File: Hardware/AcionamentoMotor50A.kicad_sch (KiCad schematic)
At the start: 56 parts, among them J1 Conn_01x02, J2 Conn_01x02, J3 Conn_01x02, Q1 IXFN420N10T, Q2 IXFN420N10T, Q3 IXFN420N10T, Q4 IXFN420N10T, U1 IXFN420N10T

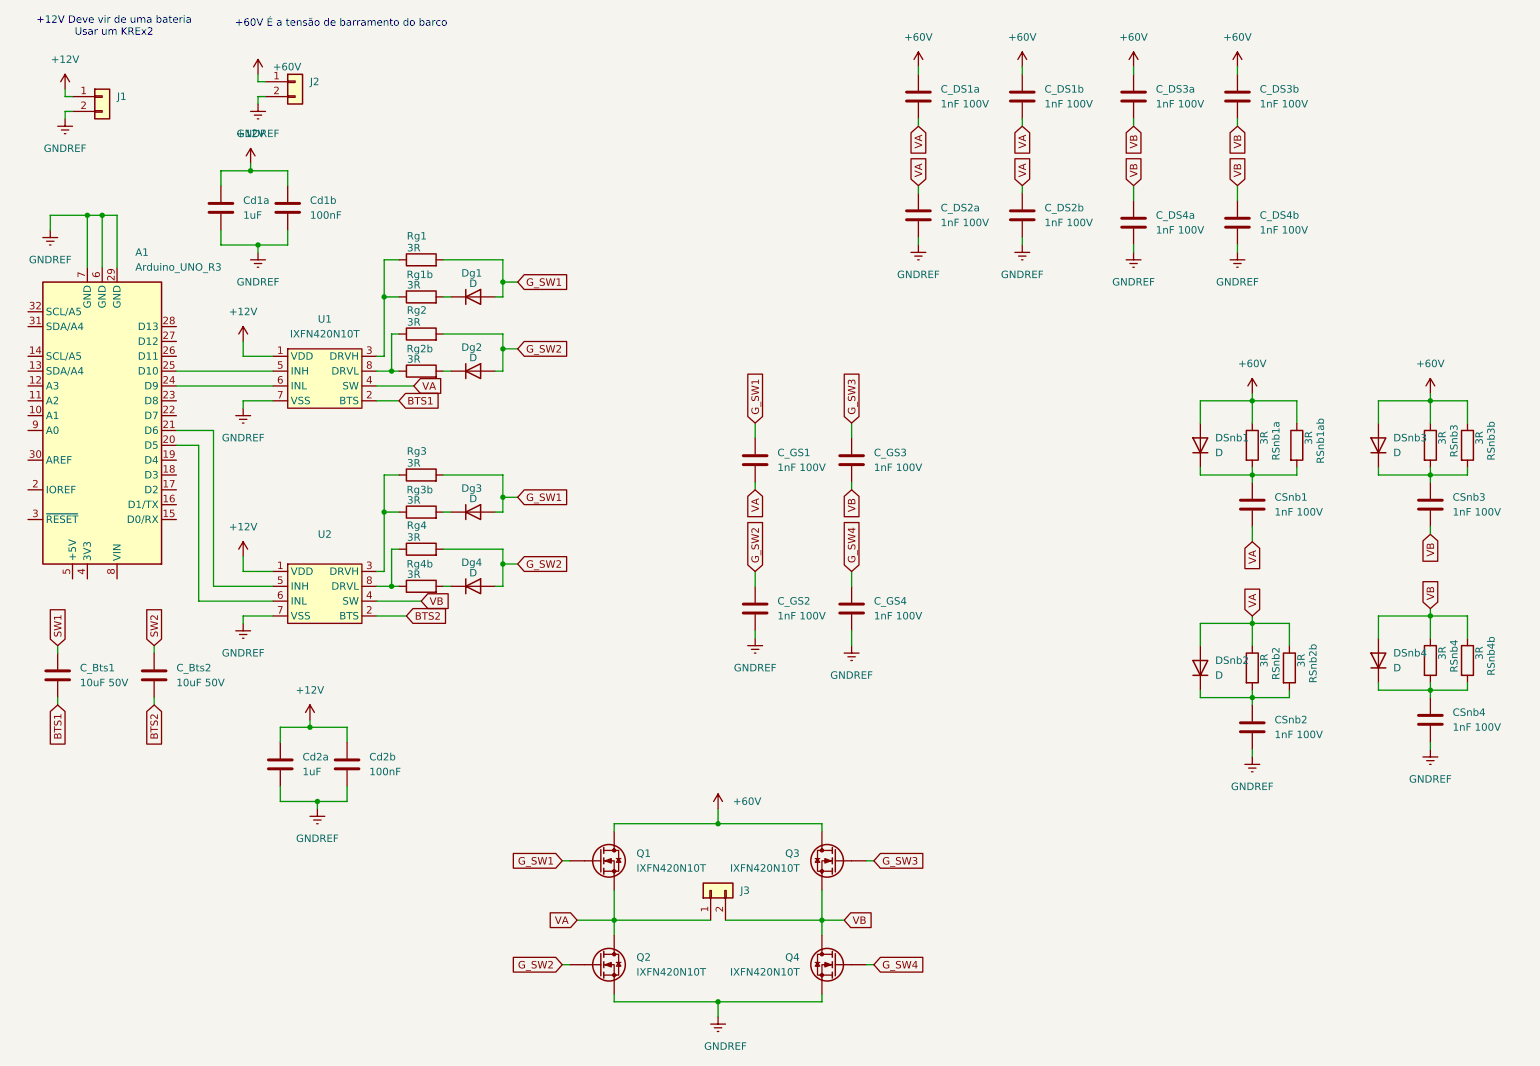
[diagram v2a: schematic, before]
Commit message: 2026_06_25
Esquemático finalizado.

Footprints corrigidos
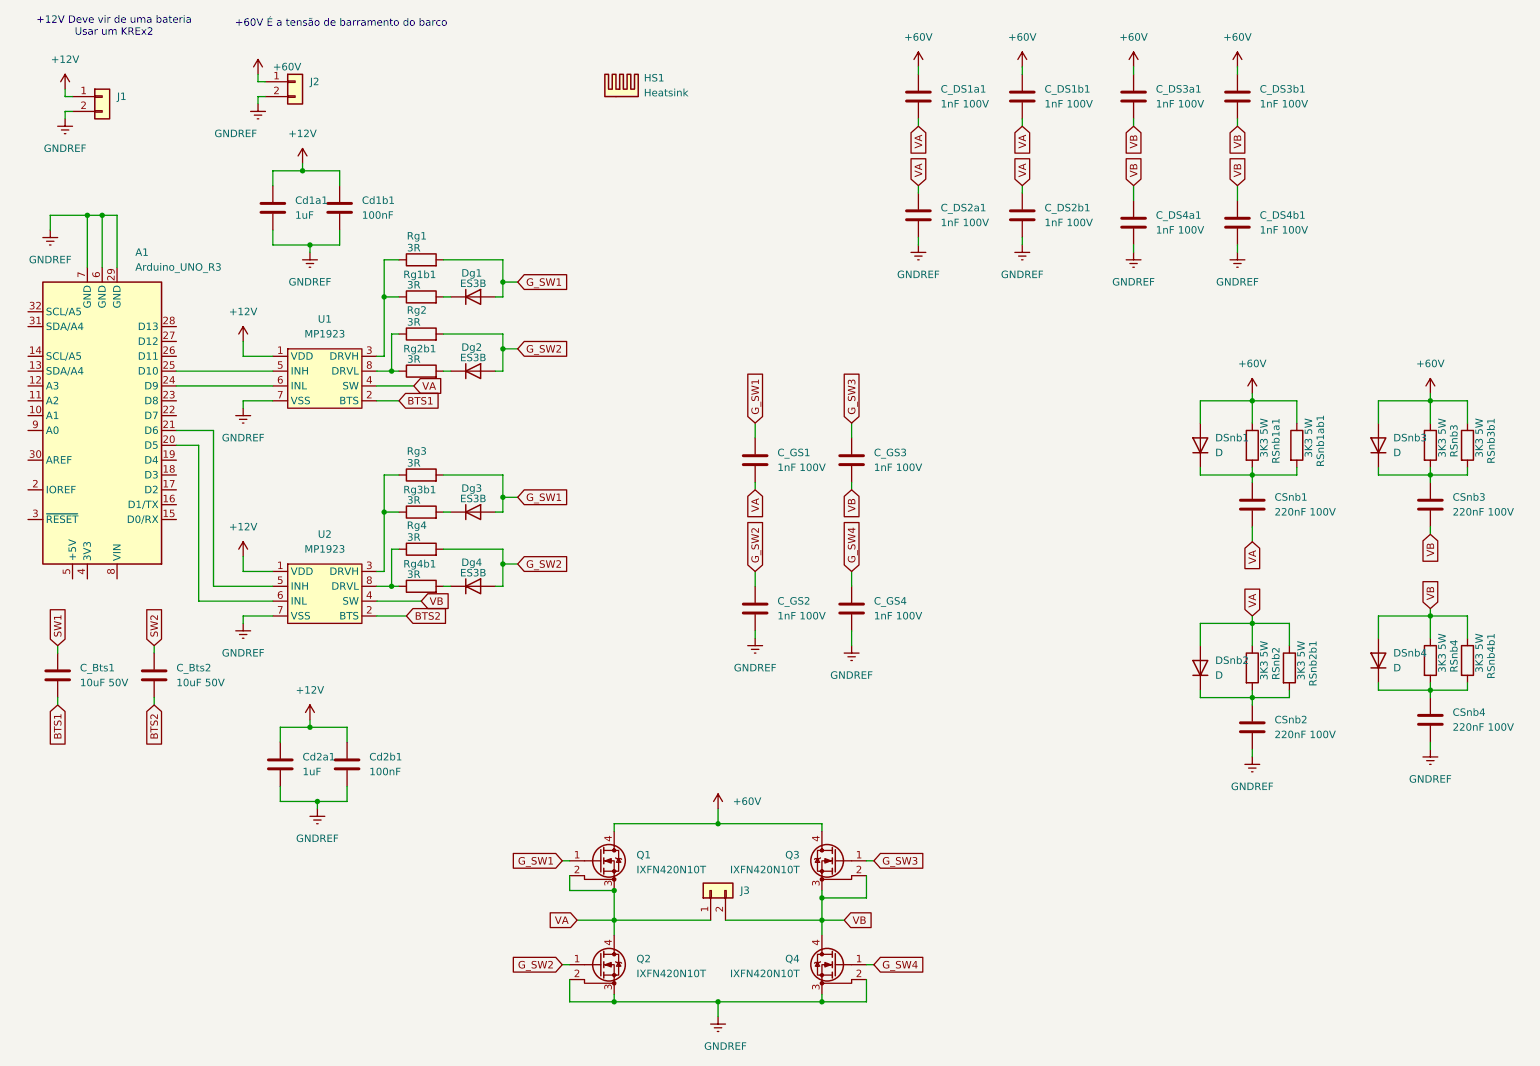
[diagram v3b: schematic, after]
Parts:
- removed Q1, Q2, Q3, Q4: IXFN420N10T, symbol Device:Q_NMOS
- added HS1: Heatsink, ZeniteSolar:Heatsink_120mmx100mm_H70mm, symbol Mechanical:Heatsink
- added Q1, Q2, Q3, Q4: IXFN420N10T, ZeniteSolar:SOT-227, symbol ZeniteSolar:IXFN420N10T
- CSnb1, CSnb2, CSnb3, CSnb4: value 1nF 100V -> 220nF 100V; footprint (none) -> Capacitor_THT:C_Axial_L5.1mm_D3.1mm_P10.00mm_Horizontal
- C_Bts1, C_Bts2, C_GS1, C_GS2, C_GS3, C_GS4: footprint (none) -> Capacitor_SMD:C_0805_2012Metric_Pad1.18x1.45mm_HandSolder
- C_DS1a1: renamed from C_DS1a; footprint (none) -> Capacitor_SMD:C_0805_2012Metric_Pad1.18x1.45mm_HandSolder
- C_DS1b1: renamed from C_DS1b; footprint (none) -> Capacitor_SMD:C_0805_2012Metric_Pad1.18x1.45mm_HandSolder
- C_DS2a1: renamed from C_DS2a; footprint (none) -> Capacitor_SMD:C_0805_2012Metric_Pad1.18x1.45mm_HandSolder
- C_DS2b1: renamed from C_DS2b; footprint (none) -> Capacitor_SMD:C_0805_2012Metric_Pad1.18x1.45mm_HandSolder
- C_DS3a1: renamed from C_DS3a; footprint (none) -> Capacitor_SMD:C_0805_2012Metric_Pad1.18x1.45mm_HandSolder
- C_DS3b1: renamed from C_DS3b; footprint (none) -> Capacitor_SMD:C_0805_2012Metric_Pad1.18x1.45mm_HandSolder
- C_DS4a1: renamed from C_DS4a; footprint (none) -> Capacitor_SMD:C_0805_2012Metric_Pad1.18x1.45mm_HandSolder
- C_DS4b1: renamed from C_DS4b; footprint (none) -> Capacitor_SMD:C_0805_2012Metric_Pad1.18x1.45mm_HandSolder
- Cd1a1: renamed from Cd1a; footprint (none) -> Capacitor_SMD:C_1206_3216Metric_Pad1.33x1.80mm_HandSolder
- Cd1b1: renamed from Cd1b; footprint (none) -> Capacitor_SMD:C_0805_2012Metric_Pad1.18x1.45mm_HandSolder
- Cd2a1: renamed from Cd2a; footprint (none) -> Capacitor_SMD:C_1206_3216Metric_Pad1.33x1.80mm_HandSolder
- Cd2b1: renamed from Cd2b; footprint (none) -> Capacitor_SMD:C_0805_2012Metric_Pad1.18x1.45mm_HandSolder
- DSnb1, DSnb2, DSnb3, DSnb4: footprint (none) -> Diode_SMD:D_SMA_Handsoldering
- Dg1, Dg2, Dg3, Dg4: value D -> ES3B; footprint (none) -> Diode_SMD:D_SMA_Handsoldering
- J1, J2, J3: footprint (none) -> TerminalBlock_Phoenix:TerminalBlock_Phoenix_MKDS-1,5-2_1x02_P5.00mm_Horizontal
- RSnb1a1: renamed from RSnb1a; value 3R -> 3K3 5W; footprint (none) -> Resistor_THT:R_Axial_Power_L25.0mm_W9.0mm_P27.94mm
- RSnb1ab1: renamed from RSnb1ab; value 3R -> 3K3 5W; footprint (none) -> Resistor_THT:R_Axial_Power_L25.0mm_W9.0mm_P27.94mm
- RSnb2, RSnb3, RSnb4: value 3R -> 3K3 5W; footprint (none) -> Resistor_THT:R_Axial_Power_L25.0mm_W9.0mm_P27.94mm
- RSnb2b1: renamed from RSnb2b; value 3R -> 3K3 5W; footprint (none) -> Resistor_THT:R_Axial_Power_L25.0mm_W9.0mm_P27.94mm
- RSnb3b1: renamed from RSnb3b; value 3R -> 3K3 5W; footprint (none) -> Resistor_THT:R_Axial_Power_L25.0mm_W9.0mm_P27.94mm
- RSnb4b1: renamed from RSnb4b; value 3R -> 3K3 5W; footprint (none) -> Resistor_THT:R_Axial_Power_L25.0mm_W9.0mm_P27.94mm
- Rg1, Rg2, Rg3, Rg4: footprint (none) -> Resistor_SMD:R_1206_3216Metric_Pad1.30x1.75mm_HandSolder
- Rg1b1: renamed from Rg1b; footprint (none) -> Resistor_SMD:R_1206_3216Metric_Pad1.30x1.75mm_HandSolder
- Rg2b1: renamed from Rg2b; footprint (none) -> Resistor_SMD:R_1206_3216Metric_Pad1.30x1.75mm_HandSolder
- Rg3b1: renamed from Rg3b; footprint (none) -> Resistor_SMD:R_1206_3216Metric_Pad1.30x1.75mm_HandSolder
- Rg4b1: renamed from Rg4b; footprint (none) -> Resistor_SMD:R_1206_3216Metric_Pad1.30x1.75mm_HandSolder
- U1: value IXFN420N10T -> MP1923; footprint (none) -> Package_SO:SOP-8_3.76x4.96mm_P1.27mm
- U2: value (none) -> MP1923; footprint (none) -> Package_SO:SOP-8_3.76x4.96mm_P1.27mm
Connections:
- net +60V: now also Q1.4 (D), Q3.4 (D)
- net GNDREF: now also Q2.2 (DS), Q2.3 (S), Q4.2 (DS), Q4.3 (S)
- net G_SW1: now also Q1.1 (G)
- net G_SW2: now also Q2.1 (G)
- net G_SW3: now also Q3.1 (G)
- net G_SW4: now also Q4.1 (G)
- net VA: now also Q1.2 (DS), Q1.3 (S), Q2.4 (D)
- net VB: now also Q3.2 (DS), Q3.3 (S), Q4.4 (D)
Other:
- moved on the sheet: Cd1a1, Cd1b1
